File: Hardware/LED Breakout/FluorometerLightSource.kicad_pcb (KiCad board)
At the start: 2 copper layers, 14 parts, among them Q1 BSS214NW, Q2 BSS214NW, Q3 BSS214NW, Q4 BSS214NW

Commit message: Layout Organization
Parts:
- moved R5 41.1 mm to (84.8, 100.6), turned to -90 degrees
- moved R4 28.9 mm to (121.9, 80.8), turned to 180 degrees
- moved D1 27.9 mm to (88.4, 111.0)
- moved Q4 26.7 mm to (112.3, 80.5)
- moved R3 26.5 mm to (107.4, 100.6), turned to 90 degrees
- moved D2 25.6 mm to (98.6, 111.0)
- moved D4 25.3 mm to (132.3, 81.3)
- moved R1 20.8 mm to (90.2, 100.6), turned to -90 degrees
- moved Q2 20.2 mm to (97.5, 88.9)
- moved Q1 20.2 mm to (88.6, 88.9)
- moved R2 20.1 mm to (98.6, 99.8), turned to 90 degrees
- moved Q3 18.2 mm to (106.4, 88.9)
- moved D3 16.8 mm to (109.0, 110.5)

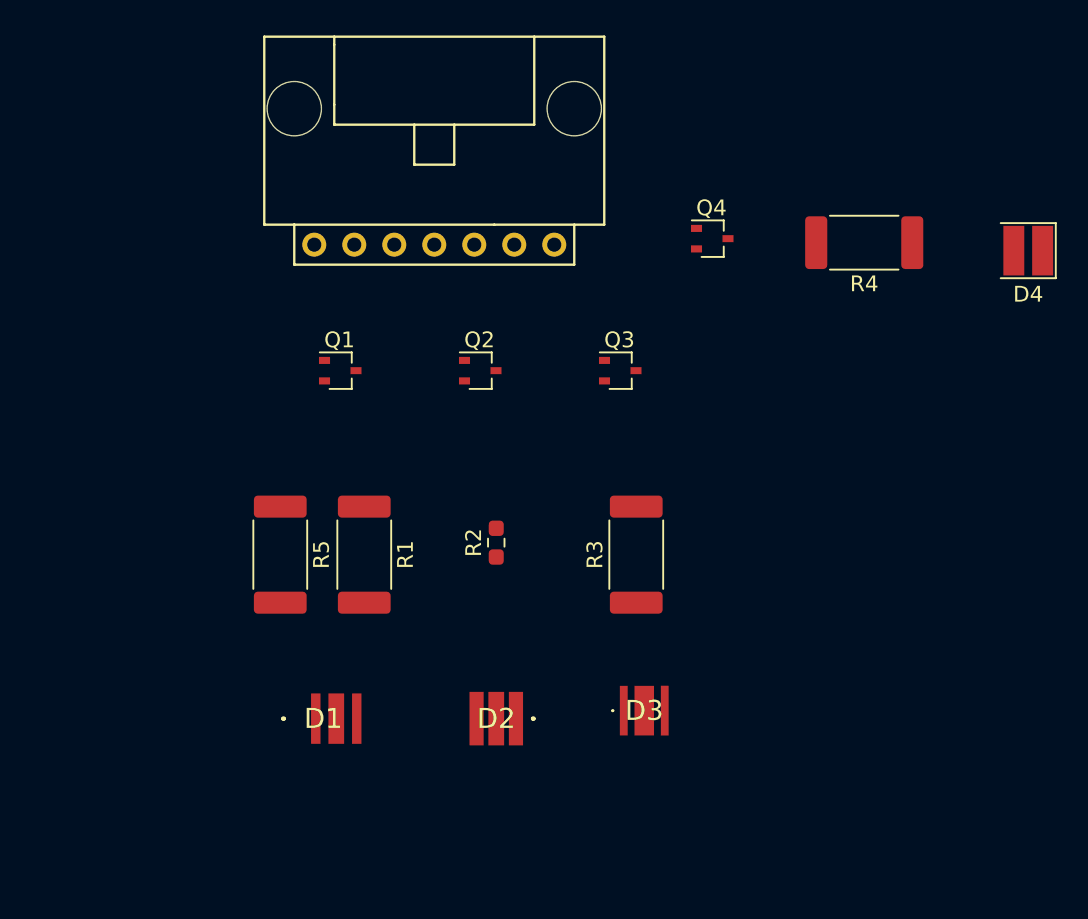
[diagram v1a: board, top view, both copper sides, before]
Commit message: Breakout rearranging, LED wiring
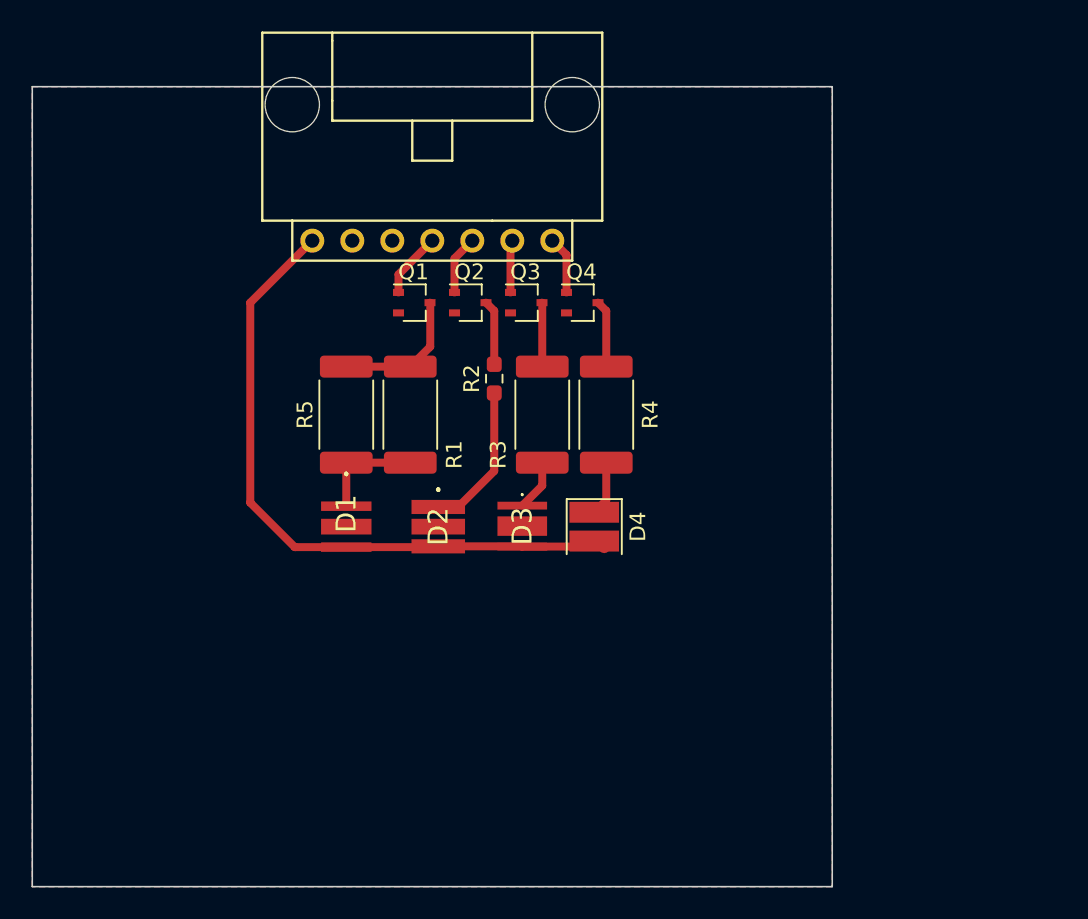
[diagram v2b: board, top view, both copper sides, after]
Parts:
- moved D4 32.7 mm to (104.8, 98.8), turned to -90 degrees
- moved R4 19.7 mm to (105.5, 91.7), turned to 90 degrees
- moved D3 13.8 mm to (100.2, 99.8), turned to -90 degrees
- moved D2 12.7 mm to (94.9, 98.8), turned to -90 degrees
- moved D1 12.2 mm to (89.0, 98.8), turned to -90 degrees
- moved R3 10.7 mm to (101.5, 91.7)
- moved R2 10.4 mm to (98.4, 89.4)
- moved R5 9.83 mm to (89.0, 91.7), turned to 90 degrees
- moved R1 9.36 mm to (93.1, 91.7), turned to 90 degrees
- moved Q4 9.20 mm to (104.0, 84.6)
- moved Q3 7.37 mm to (100.5, 84.6)
- moved Q1 6.38 mm to (93.3, 84.6)
- moved Q2 4.36 mm to (96.9, 84.6)
- moved Conn1 0.28 mm to (86.9, 80.6)
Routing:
- net +12V: track 0.00 -> 42.2 mm
- net Net-(D2-Pad1): track 0.00 -> 9.45 mm
- net Net-(Q1-Pad3): track 0.00 -> 8.66 mm
- net Net-(D1-Pad1): track 0.00 -> 6.83 mm
- net Net-(Q4-Pad3): track 0.00 -> 4.28 mm
- net Net-(Conn1-Pad4): track 0.00 -> 4.17 mm
- net Net-(Q2-Pad3): track 0.00 -> 4.13 mm
- net Net-(Q3-Pad3): track 0.00 -> 4.07 mm
- net Net-(Conn1-Pad5): track 0.00 -> 3.75 mm
- net Net-(Conn1-Pad7): track 0.00 -> 3.66 mm
- net Net-(D4-Pad1): track 0.00 -> 3.46 mm
- net Net-(Conn1-Pad6): track 0.00 -> 3.33 mm
- net Net-(D3-Pad1): track 0.00 -> 3.25 mm
- added copper zone on B.Cu, net GND
- added copper zone on F.Cu, net GND
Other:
- board outline added: 50.8 x 50.8 mm

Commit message: Breakout Boards
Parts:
- added V1: Via, MRDT_Drill_Holes:4_40_Hole, F.Cu at (109.5, 74.9)
- added V2: Via, MRDT_Drill_Holes:4_40_Hole, F.Cu at (109.5, 104.9)
- added V3: Via, MRDT_Drill_Holes:4_40_Hole, F.Cu at (79.5, 74.9)
- added V4: Via, MRDT_Drill_Holes:4_40_Hole, F.Cu at (79.5, 104.9)
- moved D3 13.3 mm to (96.2, 87.1), turned to 180 degrees
- moved R1 13.2 mm to (80.3, 88.4), turned to 0 degrees
- moved R2 12.4 mm to (86.1, 90.4), turned to 180 degrees
- moved D2 12.1 mm to (91.7, 87.1), turned to 0 degrees
- moved R5 11.4 mm to (80.3, 84.3), turned to 0 degrees
- moved Q2 10.5 mm to (86.6, 86.9)
- moved D4 9.50 mm to (97.3, 93.0), turned to 180 degrees
- moved Q1 6.77 mm to (86.6, 83.8), turned to 180 degrees
- moved D1 6.42 mm to (91.7, 93.0), turned to 0 degrees
- moved R4 4.77 mm to (109.7, 89.4)
- moved R3 4.09 mm to (105.2, 89.9)
- moved Q4 2.50 mm to (106.2, 83.3)
- moved Q3 1.59 mm to (101.9, 83.8)
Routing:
- net +12V: track 42.2 -> 28.7 mm
- net Net-(D1-Pad1): track 6.83 -> 19.1 mm
- net Net-(Conn1-Pad5): track 3.75 -> 13.7 mm
- net Net-(D4-Pad1): track 3.46 -> 13.2 mm
- net Net-(D3-Pad1): track 3.25 -> 9.46 mm
- net Net-(D2-Pad1): track 9.45 -> 4.79 mm
- net Net-(Conn1-Pad4): track 4.17 -> 8.46 mm
- net Net-(Q1-Pad3): track 8.66 -> 6.57 mm
- net Net-(Conn1-Pad7): track 3.66 -> 4.33 mm
- net GND: vias 0 -> 4
- added copper zone on F.Cu, net +12V
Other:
- board size 50.8 x 50.8 mm -> 38.1 x 38.1 mm

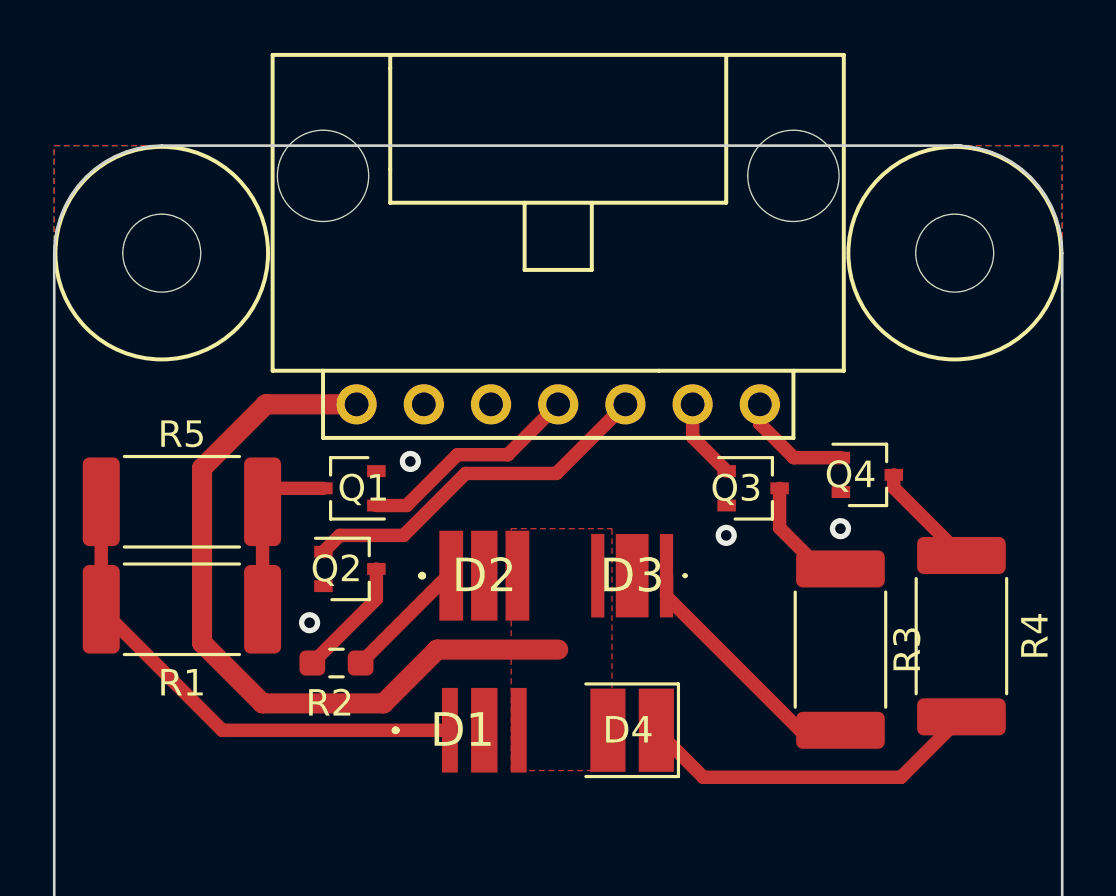
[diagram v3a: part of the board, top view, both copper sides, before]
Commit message: Changed MolexSL7 on LED breakout to SL6
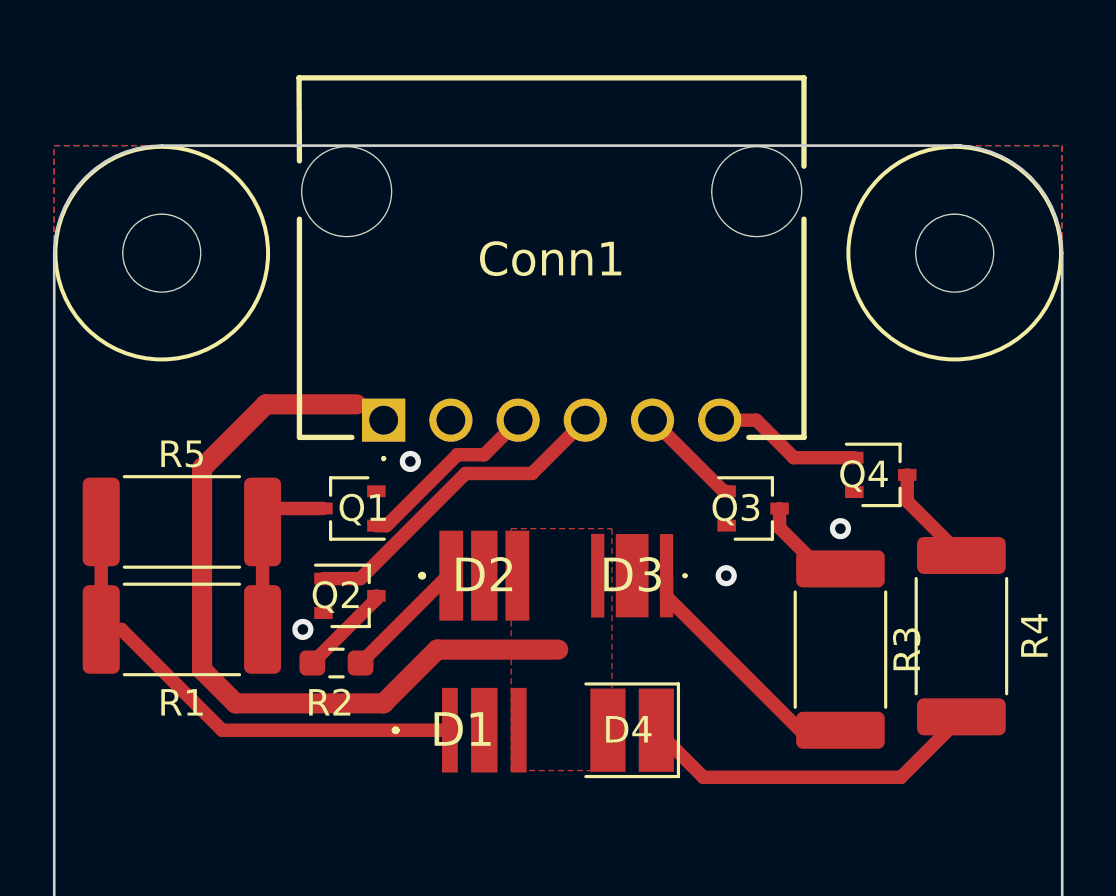
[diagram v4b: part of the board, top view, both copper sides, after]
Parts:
- Conn1: value Molex_SL_07 -> Molex_SL_06; footprint MRDT_Connectors:MOLEX_SL_07_Horizontal -> UVLEDs:705550040
- moved Conn1 1.19 mm to (87.9, 81.2), turned to 180 degrees
- moved Q2 1.02 mm to (86.6, 87.9)
- moved Q1 0.76 mm to (86.6, 84.6)
- moved Q3 0.76 mm to (101.9, 84.6)
- moved R1 0.76 mm to (80.3, 89.2)
- moved R5 0.76 mm to (80.3, 85.1)
- moved Q4 0.51 mm to (106.7, 83.3)
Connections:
- Conn1 pad 3: unconnected-(Conn1-Pad3) -> Net-(Q1-Pad1)
- Conn1 pad 4: Net-(Conn1-Pad4) -> Net-(Q2-Pad1)
- Conn1 pad 5: Net-(Conn1-Pad5) -> Net-(Q3-Pad1)
- Conn1 pad 6: Net-(Conn1-Pad6) -> Net-(Q4-Pad1)
- Q1 pad 1: Net-(Conn1-Pad4) -> Net-(Q1-Pad1)
- Q2 pad 1: Net-(Conn1-Pad5) -> Net-(Q2-Pad1)
- Q3 pad 1: Net-(Conn1-Pad6) -> Net-(Q3-Pad1)
- Q4 pad 1: Net-(Conn1-Pad7) -> Net-(Q4-Pad1)
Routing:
- net Net-(Conn1-Pad5): track 13.7 -> 0.00 mm
- net Net-(Q2-Pad1): track 0.00 -> 12.4 mm
- net Net-(Conn1-Pad4): track 8.46 -> 0.00 mm
- net Net-(Q1-Pad1): track 0.00 -> 7.03 mm
- net Net-(Q4-Pad1): track 0.00 -> 5.68 mm
- net Net-(Conn1-Pad7): track 4.33 -> 0.00 mm
- net Net-(Q3-Pad1): track 0.00 -> 3.92 mm
- net Net-(Conn1-Pad6): track 3.21 -> 0.00 mm
- net Net-(Q2-Pad3): track 4.56 -> 3.54 mm
- net Net-(Q3-Pad3): track 4.44 -> 3.68 mm
- net +12V: track 28.7 -> 29.3 mm

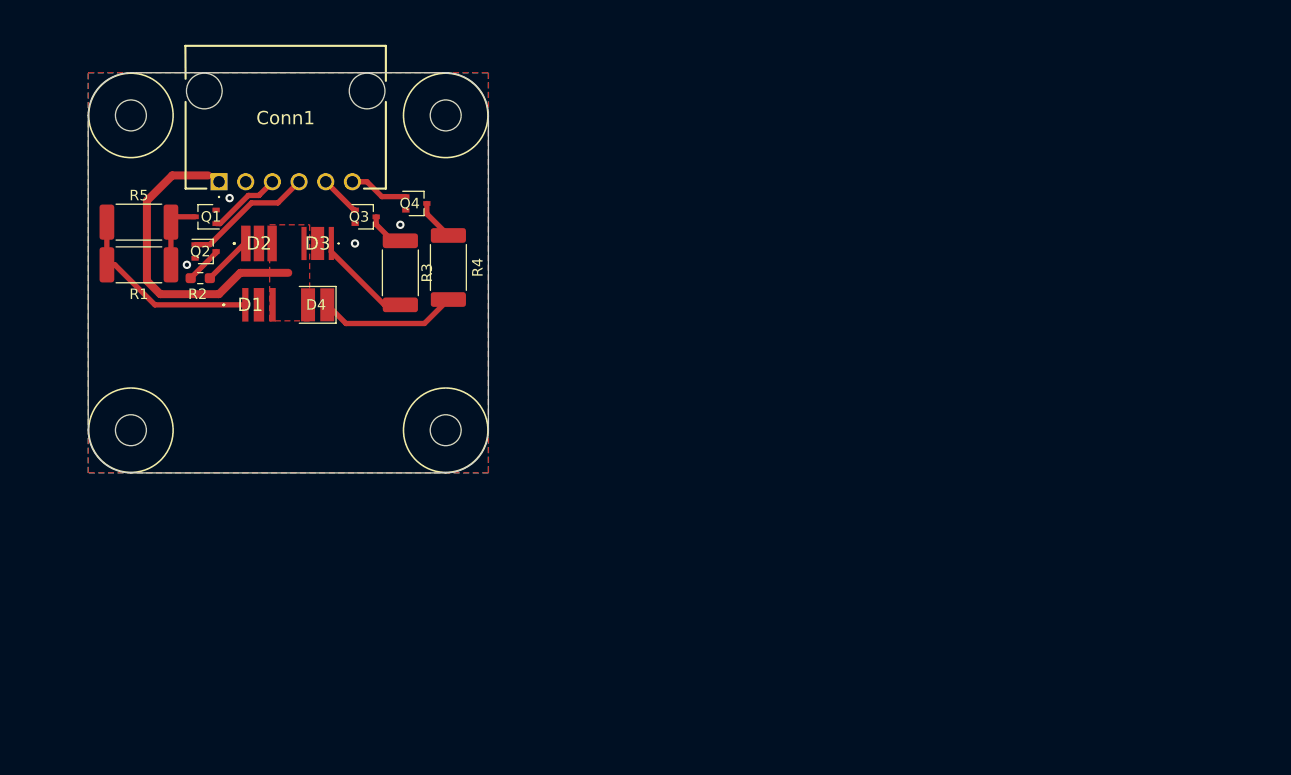
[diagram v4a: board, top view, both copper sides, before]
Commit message: Layout updated for LEDs and Science Sensor Board, schematic for CCD
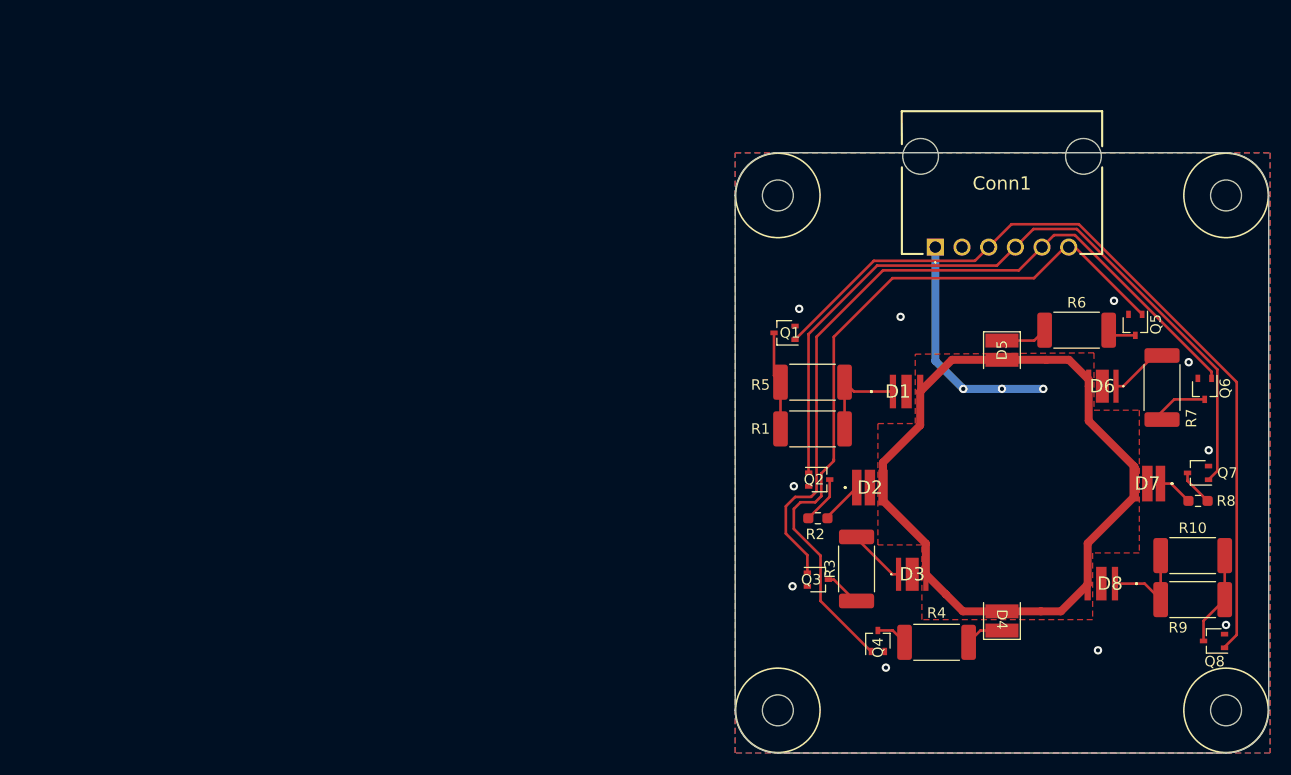
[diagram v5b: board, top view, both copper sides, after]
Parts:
- added D5: UV315, UVLEDs:WS3535C48LF-310, F.Cu at (162.4, 97.3)
- added D6: UV280, UVLEDs:XBT3535UVA130CD27501, F.Cu at (170.9, 100.7)
- added D7: UV275, UVLEDs:SUCULBN1VCAGAY674F4G30R18, F.Cu at (176.3, 110.0)
- added D8: UV260, UVLEDs:KL26550USMWD, F.Cu at (171.9, 119.5)
- added Q5: BSS214NW, Package_TO_SOT_SMD:SOT-323_SC-70, F.Cu at (175.1, 94.9)
- added Q6: BSS214NW, Package_TO_SOT_SMD:SOT-323_SC-70, F.Cu at (181.7, 101.0)
- added Q7: BSS214NW, Package_TO_SOT_SMD:SOT-323_SC-70, F.Cu at (181.1, 109.0)
- added Q8: BSS214NW, Package_TO_SOT_SMD:SOT-323_SC-70, F.Cu at (182.6, 125.0)
- added R10: 16, Resistor_SMD:R_2512_6332Metric_Pad1.40x3.35mm_HandSolder, F.Cu at (180.6, 116.8)
- added R6: 18, Resistor_SMD:R_2512_6332Metric_Pad1.40x3.35mm_HandSolder, F.Cu at (169.5, 95.4)
- added R7: 16, Resistor_SMD:R_2512_6332Metric_Pad1.40x3.35mm_HandSolder, F.Cu at (177.7, 100.8)
- added R8: 200, Resistor_SMD:R_0603_1608Metric_Pad0.98x0.95mm_HandSolder, F.Cu at (181.1, 111.6)
- added R9: 16, Resistor_SMD:R_2512_6332Metric_Pad1.40x3.35mm_HandSolder, F.Cu at (180.6, 121.0)
- moved V2 78.9 mm to (183.8, 131.6)
- moved V1 74.7 mm to (183.8, 82.5)
- moved D4 71.8 mm to (162.4, 123.1), turned to 90 degrees
- moved Conn1 68.5 mm to (156.1, 87.5)
- moved V4 67.1 mm to (141.1, 131.6)
- moved D3 66.6 mm to (154.9, 118.6), turned to 0 degrees
- moved R1 66.0 mm to (144.4, 104.8), turned to 180 degrees
- moved R5 65.9 mm to (144.4, 100.3), turned to 180 degrees
- moved R2 63.1 mm to (144.9, 113.3)
- moved D2 62.6 mm to (149.9, 110.4)
- moved Q2 62.3 mm to (145.0, 109.6)
- moved D1 62.2 mm to (153.4, 101.2)
- moved V3 62.1 mm to (141.1, 82.5)
- moved Q4 60.5 mm to (150.6, 125.0), turned to 90 degrees
- moved R4 58.6 mm to (156.2, 125.1), turned to 180 degrees
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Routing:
- net +12V: track 29.3 -> 101.9 mm, vias 0 -> 3
- net Net-(Conn1-Pad3): track 7.03 -> 78.6 mm
- net Net-(Conn1-Pad5): track 3.92 -> 73.1 mm
- net Net-(Conn1-Pad6): track 5.68 -> 70.9 mm
- net Net-(Conn1-Pad4): track 12.4 -> 72.7 mm
- net Net-(D4-Pad1): track 13.2 -> 3.64 mm
- net Net-(D1-Pad1): track 18.8 -> 9.42 mm
- net Net-(D8-Pad1): track 0.00 -> 9.17 mm
- net Net-(Q8-Pad3): track 0.00 -> 8.96 mm
- net Net-(Q6-Pad3): track 0.00 -> 5.44 mm
- net Net-(D6-Pad1): track 0.00 -> 5.01 mm
- net Net-(D5-Pad1): track 0.00 -> 4.47 mm
- net Net-(D3-Pad1): track 9.46 -> 5.55 mm
- net Net-(Q7-Pad3): track 0.00 -> 3.46 mm
- net Net-(D7-Pad1): track 0.00 -> 3.35 mm
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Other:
- board size 38.1 x 38.1 mm -> 50.8 x 57.1 mm
- board text added: "+ \ - \260\25\280\315"
- board text added: "LEDs"
